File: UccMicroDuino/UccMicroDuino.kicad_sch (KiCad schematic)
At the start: 8 parts, among them J2 Conn_01x10_Socket, J2 USB_A, U2 ATtiny85-20S

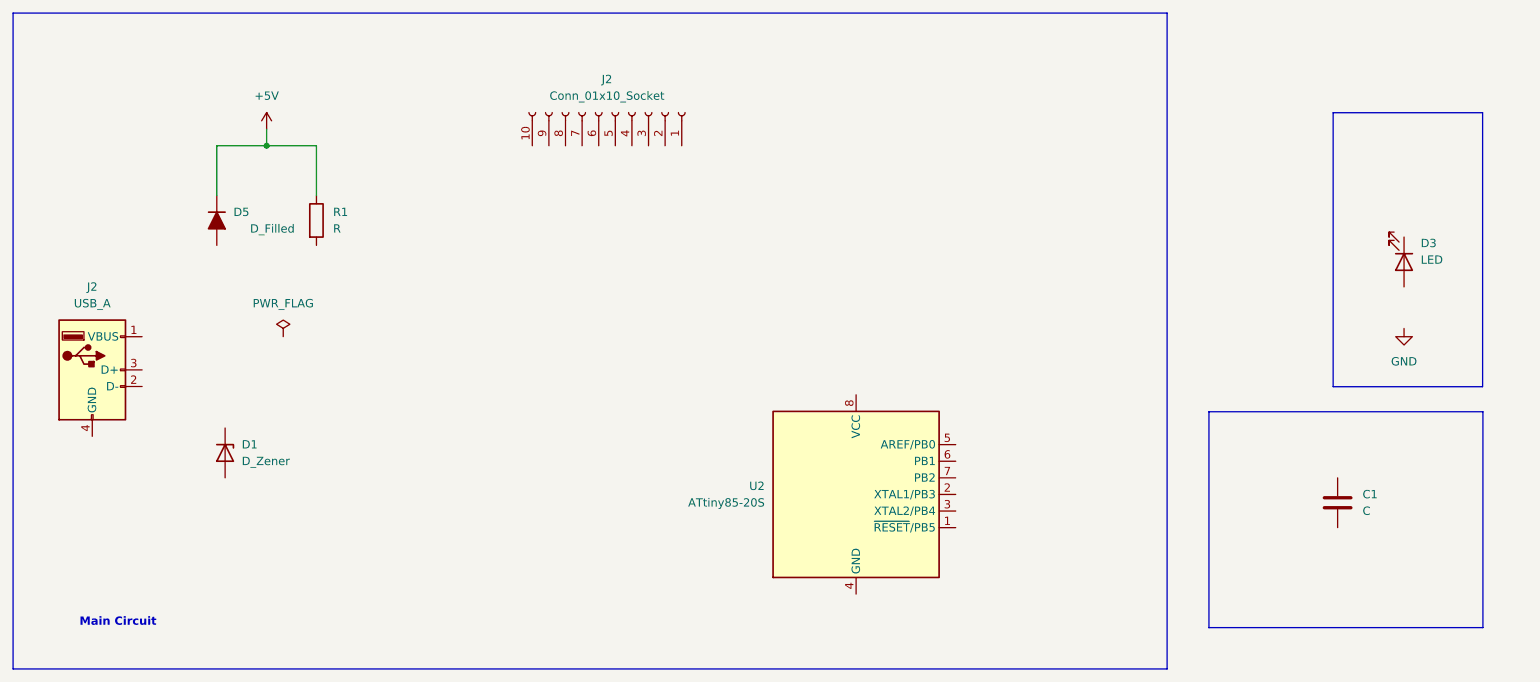
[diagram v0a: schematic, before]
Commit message: Add files via upload
Subimos el archivo kicad.
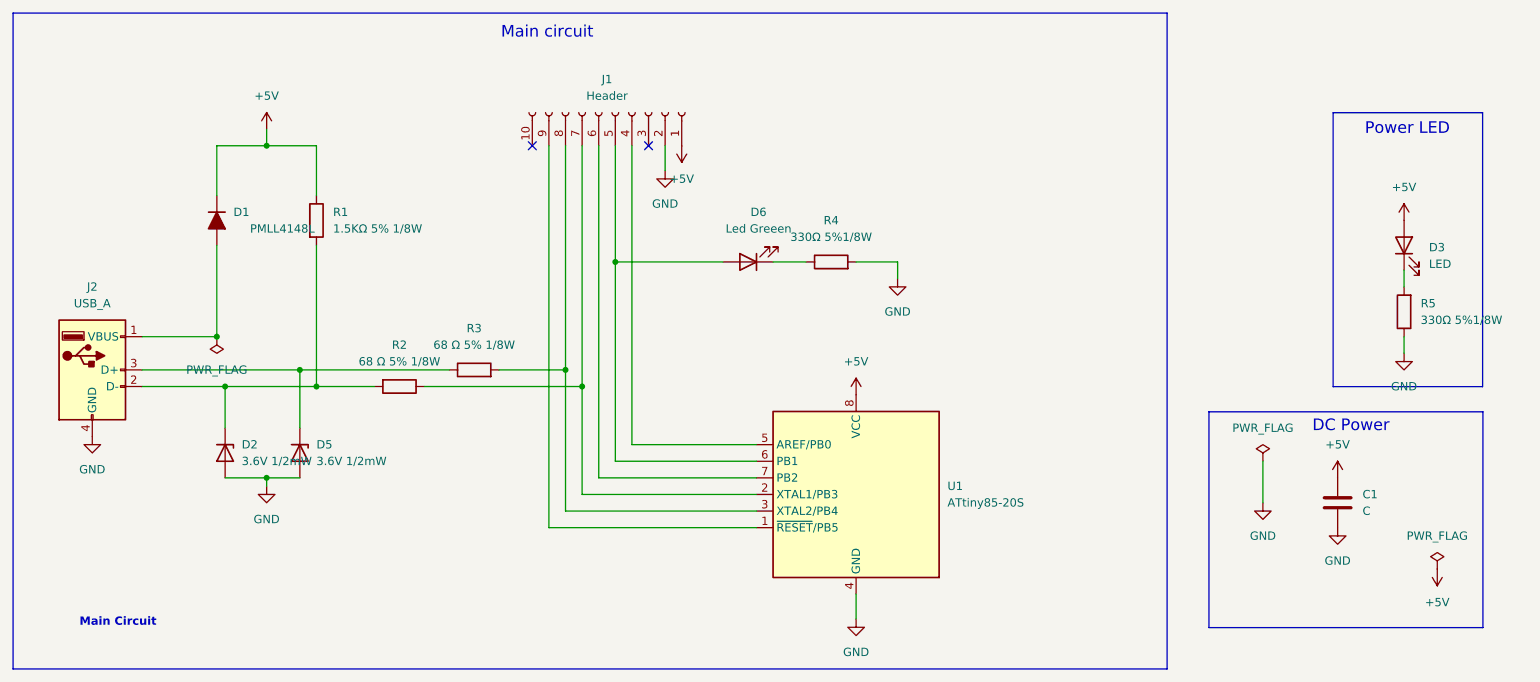
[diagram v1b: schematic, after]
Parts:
- added D5: 3.6V 1/2mW, Diode_SMD:D_SOD-123, symbol Device:D_Zener
- added D6: Led Greeen, ledSmd:ledSMD, symbol Device:LED
- added R2, R3: 68 Ω 5% 1/8W, Resistor_SMD:R_0805_2012Metric_Pad1.20x1.40mm_HandSolder, symbol Device:R
- added R4, R5: 330Ω 5%1/8W, Resistor_SMD:R_0805_2012Metric_Pad1.20x1.40mm_HandSolder, symbol Device:R
- D1: renamed from D5; value D_Filled -> PMLL4148L
- D2: renamed from D1; value D_Zener -> 3.6V 1/2mW
- J1: renamed from J2; value Conn_01x10_Socket -> Header
- R1: value R -> 1.5KΩ 5% 1/8W
- renumbered U2 to U1
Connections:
- net +5V: now also C1.1, D3.2 (A), J1.1 (Pin_1), U1.8 (VCC)
- net GND: now also C1.2, D2.2 (A), J1.2 (Pin_2), J2.4 (GND), U1.4 (GND), D5.2 (A), R4.2, R5.1
- net at D3.1 (K): now also R5.2
- net at R1.2: now also D2.1 (K), J2.2 (D-), R2.2
- net at U1.1 (~{RESET}/PB5): now also J1.9 (Pin_9)
- net at U1.2 (XTAL1/PB3): now also J1.7 (Pin_7), R2.1
- net at U1.3 (XTAL2/PB4): now also J1.8 (Pin_8), R3.2
- net at U1.5 (AREF/PB0): now also J1.4 (Pin_4)
- net at U1.6 (PB1): now also J1.5 (Pin_5), D6.2 (A)
- net at U1.7 (PB2): now also J1.6 (Pin_6)
- net at J2.1 (VBUS): now also D1.2 (A)
- net at J2.3 (D+): now also D5.1 (K), R3.1
- new net: D6.1 (K), R4.1
- no-connect marks 0 -> 2
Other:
- note added: "DC Power"
- note added: "Main circuit"
- note added: "Power LED"
- moved on the sheet: D3, U1
